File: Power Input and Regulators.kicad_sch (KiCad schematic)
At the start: 26 parts, among them J403 Screw_Terminal_01x03, U11 LD1117S33TR_SOT223, U12 LD1117S18TR_SOT223

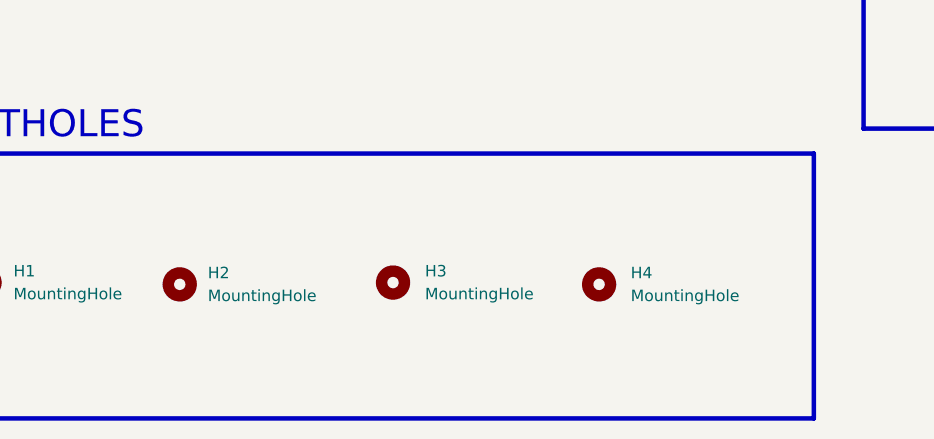
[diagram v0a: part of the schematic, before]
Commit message: ethernet, debugger and usb layouts re-designed
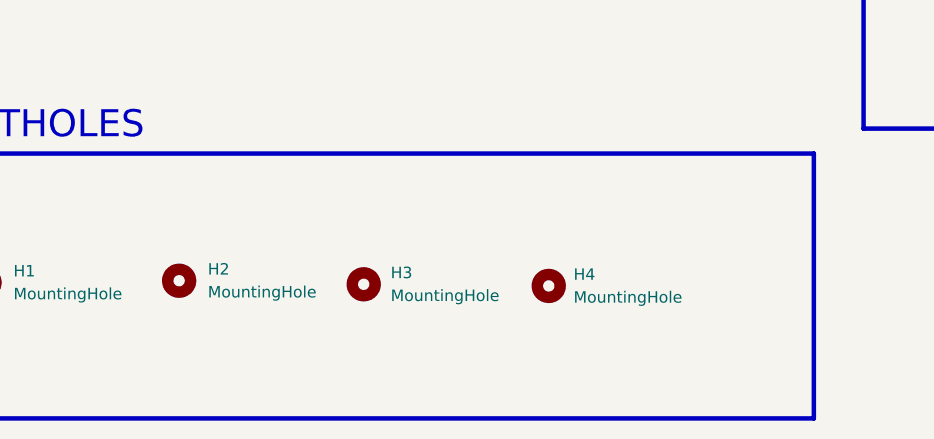
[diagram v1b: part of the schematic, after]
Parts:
- H1, H2, H3, H4: footprint MountingHole:MountingHole_2.1mm -> MountingHole:MountingHole_2.2mm_M2_ISO7380_Pad

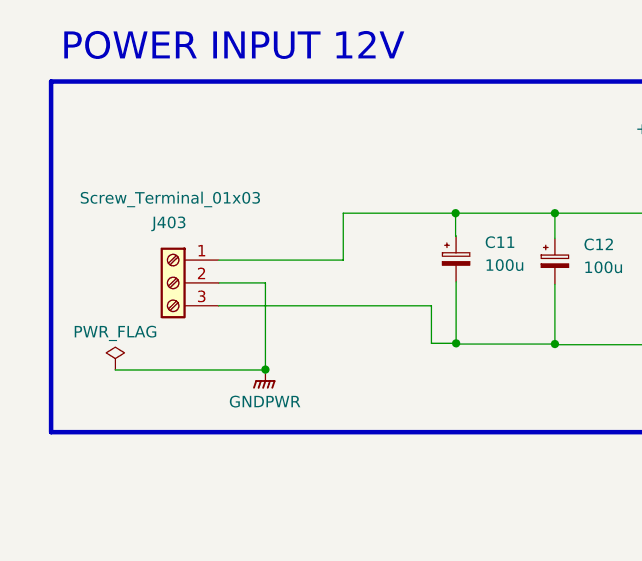
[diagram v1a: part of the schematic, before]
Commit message: all layouts re-designed.Next step routing...
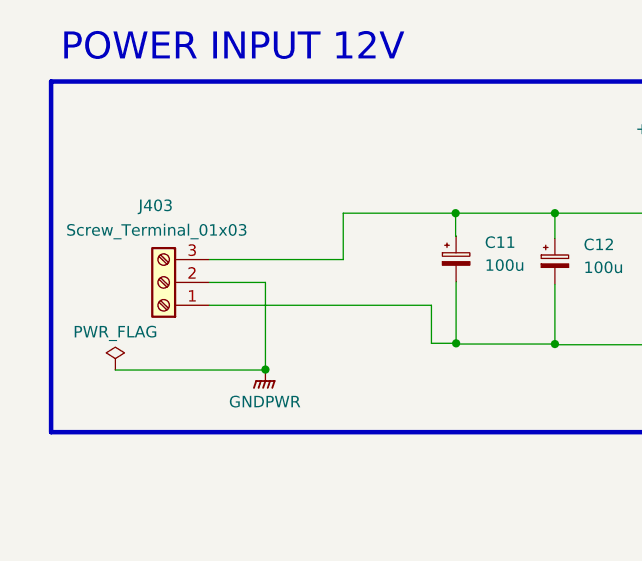
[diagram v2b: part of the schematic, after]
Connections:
- net +12V: now also J403.3 (Pin_3); no longer J403.1 (Pin_1)
- net GND: now also J403.1 (Pin_1); no longer J403.3 (Pin_3)
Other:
- moved on the sheet: J403
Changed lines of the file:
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@@
 	(wire
 		(pts
-			(xy 67.1027 52.1348) (xy 67.1027 57.3452)
+			(xy 67.1027 52.1348) (xy 67.1027 57.2872)
 		)
 		(stroke
@@
 	(wire
 		(pts
-			(xy 53.2822 62.4252) (xy 76.9003 62.4252)
+			(xy 52.2294 62.3672) (xy 76.9003 62.3672)
 		)
 		(stroke
@@
 	(wire
 		(pts
-			(xy 67.1027 57.3452) (xy 53.2822 57.3452)
+			(xy 67.1027 57.2872) (xy 52.2294 57.2872)
 		)
 		(stroke
@@
 	(wire
 		(pts
-			(xy 53.2822 59.8852) (xy 58.4554 59.8852)
+			(xy 52.2294 59.8272) (xy 58.4554 59.8272)
 		)
 		(stroke
@@
 	(wire
 		(pts
-			(xy 76.9003 62.4252) (xy 76.9003 66.5943)
+			(xy 76.9003 62.3672) (xy 76.9003 66.5943)
 		)
 		(stroke
@@
 	(wire
 		(pts
-			(xy 58.4554 59.8852) (xy 58.4554 69.5105)
+			(xy 58.4554 59.8272) (xy 58.4554 69.5105)
 		)
 		(stroke
@@
 	(symbol
 		(lib_id "Connector:Screw_Terminal_01x03")
-		(at 48.2022 59.8852 0)
-		(mirror y)
+		(at 47.1494 59.8272 180)
 		(unit 1)
 		(exclude_from_sim no)
@@
 		(dnp no)
 		(property "Reference" "J403"
-			(at 47.7823 53.2066 0)
+			(at 46.2706 51.3095 0)
 			(effects
 				(font
@@
 		)
 		(property "Value" "Screw_Terminal_01x03"
-			(at 47.9064 50.4752 0)
+			(at 46.3947 54.0409 0)
 			(effects
 				(font
@@
 		)
 		(property "Footprint" "TerminalBlock_Phoenix:TerminalBlock_Phoenix_PT-1,5-3-5.0-H_1x03_P5.00mm_Horizontal"
-			(at 48.2022 59.8852 0)
+			(at 47.1494 59.8272 0)
 			(effects
 				(font
@@
 		)
 		(property "Datasheet" "~"
-			(at 48.2022 59.8852 0)
+			(at 47.1494 59.8272 0)
 			(effects
 				(font
@@
 		)
 		(property "Description" "Generic screw terminal, single row, 01x03, script generated (kicad-library-utils/schlib/autogen/connector/)"
-			(at 48.2022 59.8852 0)
+			(at 47.1494 59.8272 0)
 			(effects
 				(font

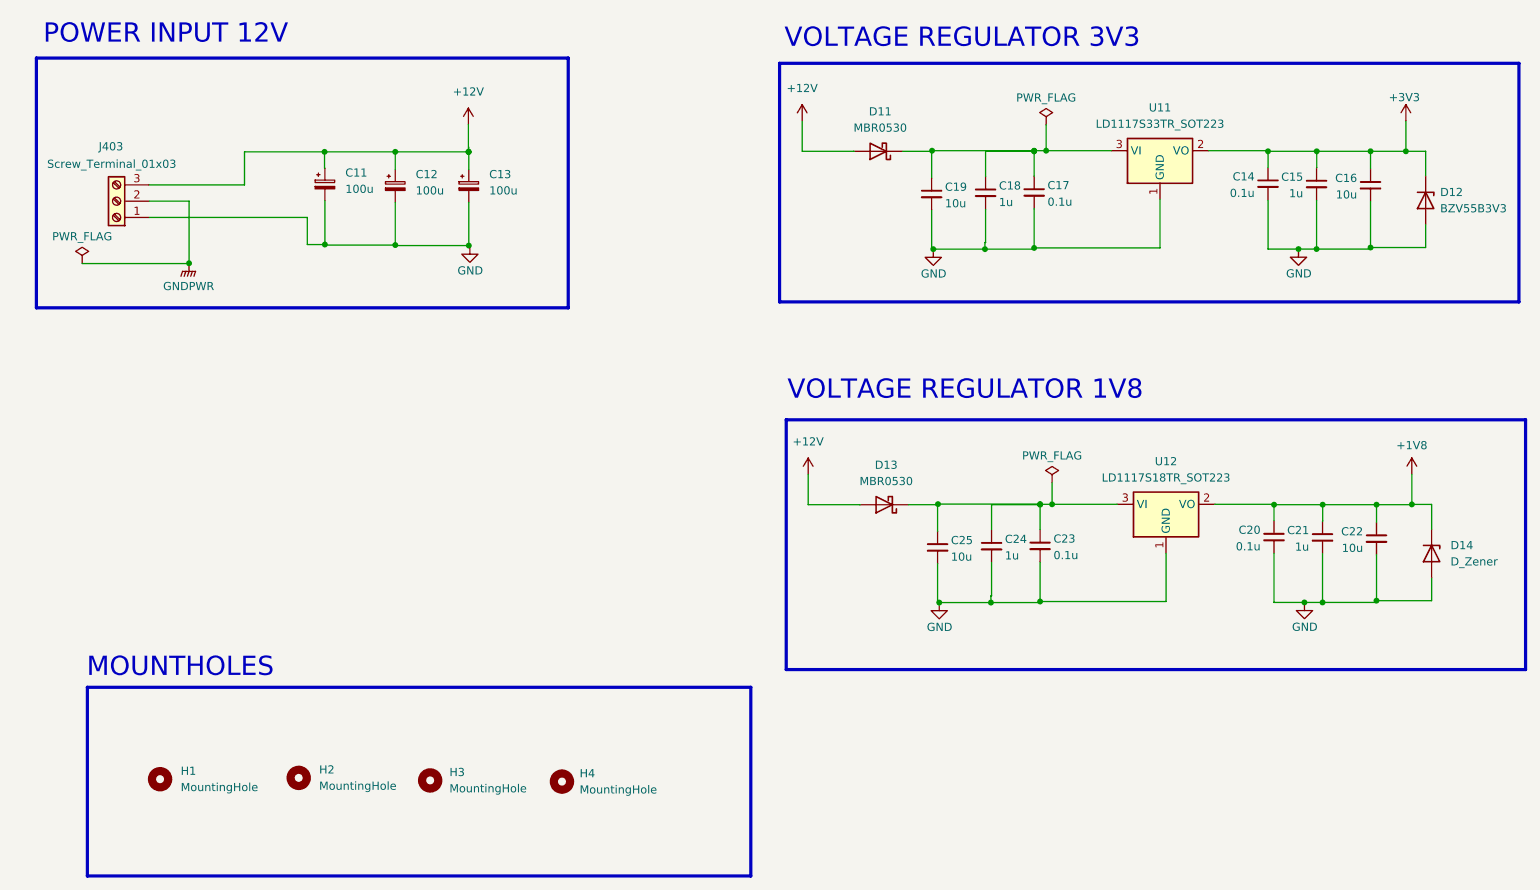
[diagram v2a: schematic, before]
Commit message: all tracks routed, ERC checked, silkscreens reviewed. Next step is PDN Analysis
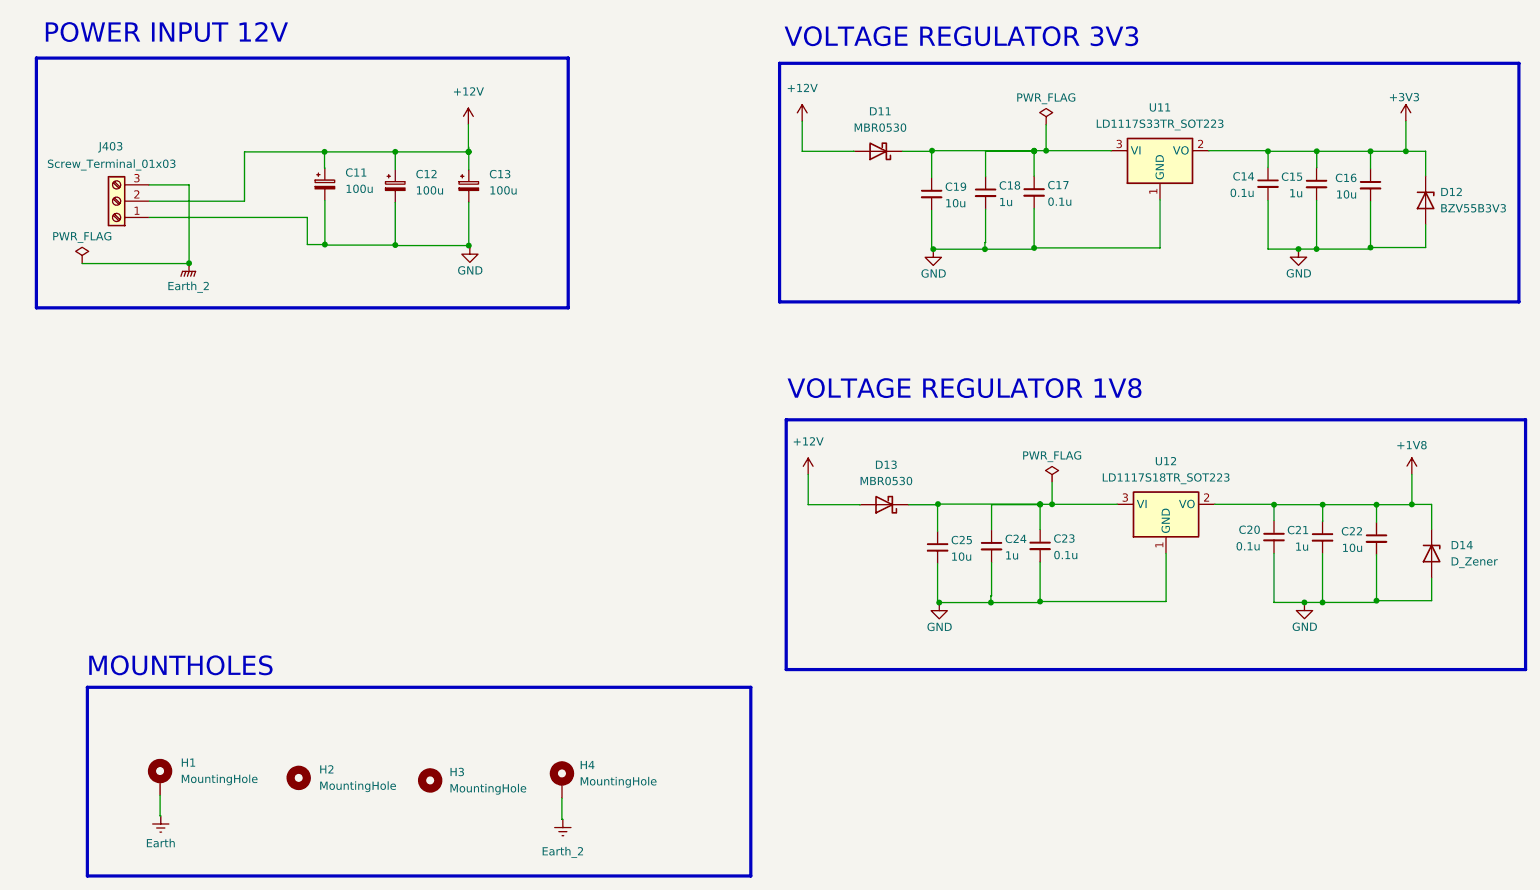
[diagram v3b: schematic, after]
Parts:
- H1, H4: symbol Mechanical:MountingHole -> Mechanical:MountingHole_Pad; now left out of the parts list
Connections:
- net GNDPWR is gone; now on net +12V: J403.2 (Pin_2)
- net +12V: no longer J403.3 (Pin_3)
- new net Earth: H1.1
- new net Earth_2: H4.1, J403.3 (Pin_3)
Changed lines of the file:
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@@
 	(wire
 		(pts
-			(xy 67.1027 52.1348) (xy 67.1027 57.2872)
+			(xy 58.4554 57.2872) (xy 58.4554 69.5105)
+		)
+		(stroke
+			(width 0)
+			(type default)
+		)
+	)
+	(wire
+		(pts
+			(xy 67.1027 52.1348) (xy 67.1027 59.8272)
 		)
 		(stroke
@@
 	(wire
 		(pts
+			(xy 116.6243 156.2703) (xy 116.7642 156.2703)
+		)
+		(stroke
+			(width 0)
+			(type default)
+		)
+	)
+	(wire
+		(pts
 			(xy 102.0265 52.1348) (xy 102.0898 52.1348)
 		)
@@
 	(wire
 		(pts
-			(xy 67.1027 57.2872) (xy 52.2294 57.2872)
-		)
-		(stroke
-			(width 0)
-			(type default)
-		)
-	)
-	(wire
-		(pts
 			(xy 79.5868 52.1348) (xy 90.6209 52.1348)
 		)
@@
 	(wire
 		(pts
+			(xy 52.2294 57.2872) (xy 58.4554 57.2872)
+		)
+		(stroke
+			(width 0)
+			(type default)
+		)
+	)
+	(wire
+		(pts
 			(xy 191.2089 116.1368) (xy 191.2089 122.2781)
 		)
@@
 	(wire
 		(pts
-			(xy 52.2294 59.8272) (xy 58.4554 59.8272)
+			(xy 251.3486 67.0595) (xy 242.7543 67.0595)
 		)
 		(stroke
@@
 	(wire
 		(pts
-			(xy 251.3486 67.0595) (xy 242.7543 67.0595)
+			(xy 175.2177 107.0809) (xy 175.2838 107.0809)
 		)
 		(stroke
@@
 	(wire
 		(pts
-			(xy 175.2177 107.0809) (xy 175.2838 107.0809)
+			(xy 116.6243 152.9093) (xy 116.6243 156.2703)
 		)
 		(stroke
@@
 	(wire
 		(pts
+			(xy 52.2294 59.8272) (xy 67.1027 59.8272)
+		)
+		(stroke
+			(width 0)
+			(type default)
+		)
+	)
+	(wire
+		(pts
 			(xy 155.0312 102.4533) (xy 155.0312 107.1722)
 		)
@@
 	(wire
 		(pts
-			(xy 58.4554 59.8272) (xy 58.4554 69.5105)
+			(xy 175.2177 116.3775) (xy 175.2177 122.441)
 		)
 		(stroke
@@
 	(wire
 		(pts
-			(xy 175.2177 116.3775) (xy 175.2177 122.441)
+			(xy 53.934 155.7094) (xy 54.0411 155.7094)
 		)
 		(stroke
@@
 	(wire
 		(pts
+			(xy 53.934 152.5341) (xy 53.934 155.7094)
+		)
+		(stroke
+			(width 0)
+			(type default)
+		)
+	)
+	(wire
+		(pts
 			(xy 243.6847 107.1732) (xy 235.2911 107.1732)
 		)
@@
 	)
 	(symbol
-		(lib_id "Mechanical:MountingHole")
+		(lib_id "Mechanical:MountingHole_Pad")
 		(at 116.6243 150.3693 0)
 		(unit 1)
-		(exclude_from_sim no)
-		(in_bom yes)
+		(exclude_from_sim yes)
+		(in_bom no)
 		(on_board yes)
 		(dnp no)
 		(fields_autoplaced yes)
 		(property "Reference" "H4"
-			(at 119.38 149.0992 0)
+			(at 119.38 147.8292 0)
 			(effects
 				(font
@@
 		)
 		(property "Value" "MountingHole"
-			(at 119.38 151.6392 0)
+			(at 119.38 150.3692 0)
 			(effects
 				(font
@@
 			)
 		)
-		(property "Description" "Mounting Hole without connection"
+		(property "Description" "Mounting Hole with connection"
 			(at 116.6243 150.3693 0)
 			(effects
@@
 			)
 		)
+		(pin "1"
+		)
 		(instances
 			(project "mixed signal board project"
@@
 	)
 	(symbol
+		(lib_id "power:Earth")
+		(at 54.0411 155.7094 0)
+		(unit 1)
+		(exclude_from_sim no)
+		(in_bom yes)
+		(on_board yes)
+		(dnp no)
+		(fields_autoplaced yes)
+		(property "Reference" "#PWR0507"
+			(at 54.0411 162.0594 0)
+			(effects
+				(font
+					(size 1.27 1.27)
+				)
+				(hide yes)
+			)
+		)
+		(property "Value" "Earth"
+			(at 54.0411 160.02 0)
+			(effects
+				(font
+					(size 1.27 1.27)
+				)
+			)
+		)
+		(property "Footprint" ""
+			(at 54.0411 155.7094 0)
+			(effects
+				(font
+					(size 1.27 1.27)
+				)
+				(hide yes)
+			)
+		)
+		(property "Datasheet" "~"
+			(at 54.0411 155.7094 0)
+			(effects
+				(font
+					(size 1.27 1.27)
+				)
+				(hide yes)
+			)
+		)
+		(property "Description" "Power symbol creates a global label with name \"Earth\""
+			(at 54.0411 155.7094 0)
+			(effects
+				(font
+					(size 1.27 1.27)
+				)
+				(hide yes)
+			)
+		)
+		(pin "1"
+		)
+		(instances
+			(project ""
+				(path "/8a424437-6f3e-424c-a786-3b8b285eee60/89ed5f6c-6a59-4754-9fdb-29c83f804302"
+					(reference "#PWR0507")
+					(unit 1)
+				)
+			)
+		)
+	)
+	(symbol
 		(lib_id "Device:C_Small")
 		(at 174.2873 58.7112 0)
@@
 	)
 	(symbol
-		(lib_id "Mechanical:MountingHole")
+		(lib_id "Mechanical:MountingHole_Pad")
 		(at 53.934 149.9941 0)
 		(unit 1)
-		(exclude_from_sim no)
-		(in_bom yes)
+		(exclude_from_sim yes)
+		(in_bom no)
 		(on_board yes)
 		(dnp no)
 		(fields_autoplaced yes)
 		(property "Reference" "H1"
-			(at 57.15 148.724 0)
+			(at 57.15 147.454 0)
 			(effects
 				(font
@@
 		)
 		(property "Value" "MountingHole"
-			(at 57.15 151.264 0)
+			(at 57.15 149.994 0)
 			(effects
 				(font
@@
 			)
 		)
-		(property "Description" "Mounting Hole without connection"
+		(property "Description" "Mounting Hole with connection"
 			(at 53.934 149.9941 0)
 			(effects
@@
 			)
 		)
+		(pin "1"
+		)
 		(instances
 			(project ""
@@
 	)
 	(symbol
+		(lib_id "power:Earth")
+		(at 116.7642 156.2703 0)
+		(unit 1)
+		(exclude_from_sim no)
+		(in_bom yes)
+		(on_board yes)
+		(dnp no)
+		(fields_autoplaced yes)
+		(property "Reference" "#PWR0508"
+			(at 116.7642 162.6203 0)
+			(effects
+				(font
+					(size 1.27 1.27)
+				)
+				(hide yes)
+			)
+		)
+		(property "Value" "Earth_2"
+			(at 116.7642 161.29 0)
+			(effects
+				(font
+					(size 1.27 1.27)
+				)
+			)
+		)
+		(property "Footprint" ""
+			(at 116.7642 156.2703 0)
+			(effects
+				(font
+					(size 1.27 1.27)
+				)
+				(hide yes)
+			)
+		)
+		(property "Datasheet" "~"
+			(at 116.7642 156.2703 0)
+			(effects
+				(font
+					(size 1.27 1.27)
+				)
+				(hide yes)
+			)
+		)
+		(property "Description" "Power symbol creates a global label with name \"Earth\""
+			(at 116.7642 156.2703 0)
+			(effects
+				(font
+					(size 1.27 1.27)
+				)
+				(hide yes)
+			)
+		)
+		(pin "1"
+		)
+		(instances
+			(project "mixed signal board project"
+				(path "/8a424437-6f3e-424c-a786-3b8b285eee60/89ed5f6c-6a59-4754-9fdb-29c83f804302"
+					(reference "#PWR0508")
+					(unit 1)
+				)
+			)
+		)
+	)
+	(symbol
 		(lib_id "power:GNDPWR")
 		(at 58.4554 69.5105 0)
@@
 			)
 		)
-		(property "Value" "GNDPWR"
+		(property "Value" "Earth_2"
 			(at 58.3919 73.1131 0)
 			(effects

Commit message: some additions
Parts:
- renumbered C17 to C?, C16 to C?, C14 to C?, C23 to C?, C21 to C?, C25 to C?, C24 to C?, C12 to C?, C11 to C?, C22 to C?, C15 to C?, C18 to C?, C13 to C?, C19 to C?, C20 to C?, D12 to D?, D13 to D?, D11 to D?, D14 to D?, H3 to H?, H4 to H?, H1 to H?, H2 to H?, J403 to J?, U11 to U?, U12 to U?
